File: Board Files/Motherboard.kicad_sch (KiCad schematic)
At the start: 121 parts, among them P1 72-Pin Connector, P2 EXP-Connector, P3 MOD RF, P4 Controller Input, P5 Controller Input, P6 PWR/RST IN, Q1 2SA937, Q2 2SC2021, Q3 2SC2021, U1 6116 (WRAM), U10 CIC, U2 74HC373, U3 74HC139, U4 6116 (VRAM), U5 RP2C02 PPU, U6 RP2A03 CPU, U7 40H368 (CI), U8 40H368 (CII), U9 74LS04, X1 21.477272 MHz, X2 4MHz

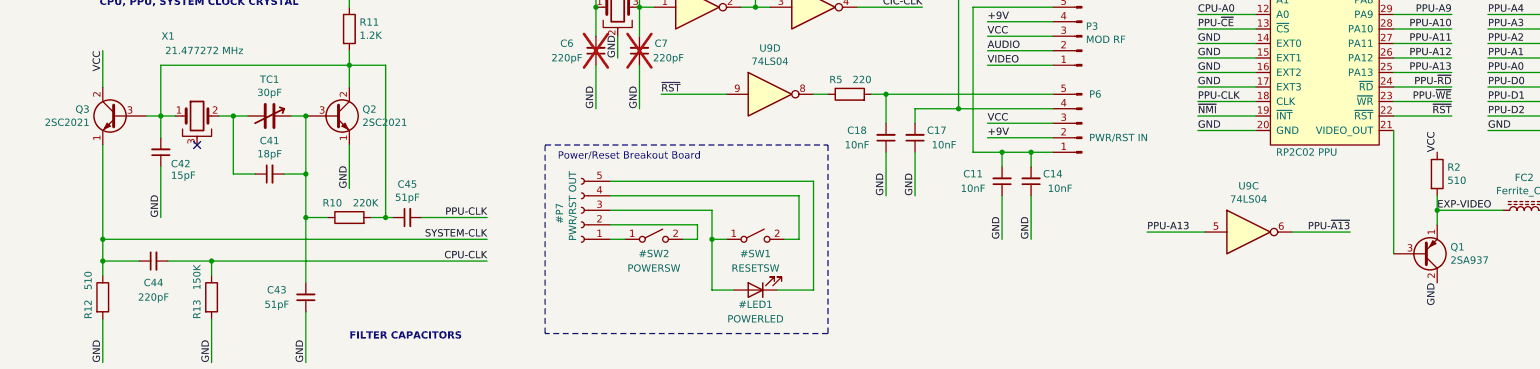
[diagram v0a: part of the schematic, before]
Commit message: fix: 74HC368 bus pin type
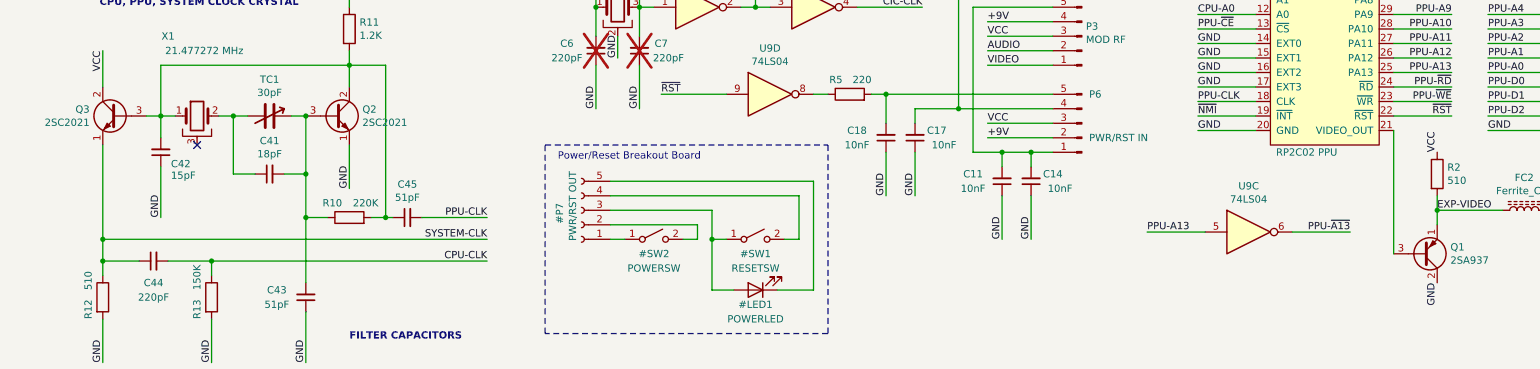
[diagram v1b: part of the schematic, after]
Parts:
- Q1: symbol Device:Q_PNP_ECB -> Transistor_BJT:Q_PNP_ECB
- Q2, Q3: symbol Device:Q_NPN_ECB -> Transistor_BJT:Q_NPN_ECB
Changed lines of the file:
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@@
 	)
 	(symbol
-		(lib_id "Device:Q_PNP_ECB")
+		(lib_id "Transistor_BJT:Q_PNP_ECB")
 		(at 267.97 215.9 0)
 		(mirror x)
@@
 			)
 		)
-		(property "Description" ""
+		(property "Description" "PNP transistor, emitter/collector/base"
 			(at 267.97 215.9 0)
 			(effects
@@
 	)
 	(symbol
-		(lib_id "Device:Q_NPN_ECB")
+		(lib_id "Transistor_BJT:Q_NPN_ECB")
 		(at 77.47 191.77 0)
 		(unit 1)
@@
 			)
 		)
-		(property "Description" ""
+		(property "Description" "NPN transistor, emitter/collector/base"
 			(at 77.47 191.77 0)
 			(effects
@@
 	)
 	(symbol
-		(lib_id "Device:Q_NPN_ECB")
+		(lib_id "Transistor_BJT:Q_NPN_ECB")
 		(at 39.37 191.77 0)
 		(mirror y)
@@
 			)
 		)
-		(property "Description" ""
+		(property "Description" "NPN transistor, emitter/collector/base"
 			(at 39.37 191.77 0)
 			(effects
@@
 			)
 		)
-		(property "Description" ""
+		(property "Description" "Light emitting diode"
+			(at 151.13 222.25 0)
+			(effects
+				(font
+					(size 1.27 1.27)
+				)
+				(hide yes)
+			)
+		)
+		(property "Sim.Pins" "1=K 2=A"
 			(at 151.13 222.25 0)
 			(effects

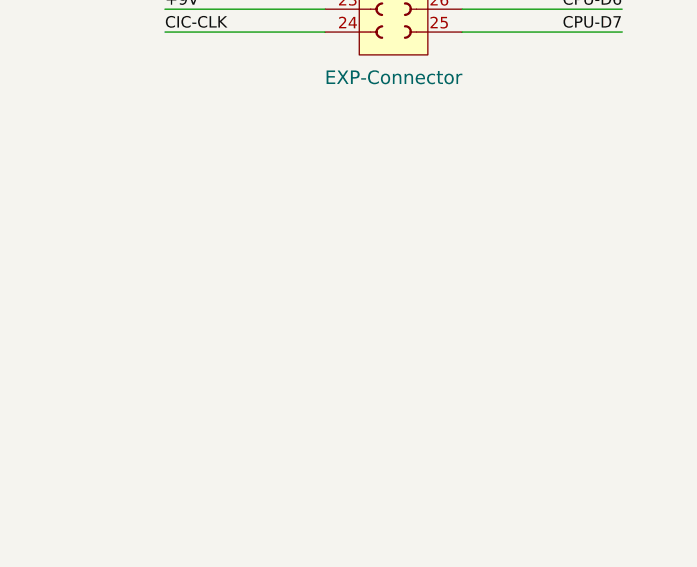
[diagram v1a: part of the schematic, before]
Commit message: feat: added power flag to gnd and vcc nets
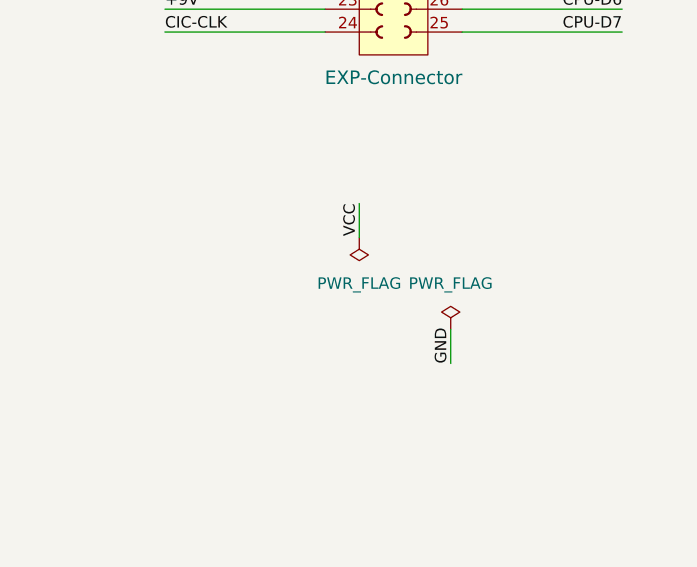
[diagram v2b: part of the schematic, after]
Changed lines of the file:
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@@
 	(wire
 		(pts
+			(xy 368.3 232.41) (xy 368.3 236.22)
+		)
+		(stroke
+			(width 0)
+			(type default)
+		)
+	)
+	(wire
+		(pts
 			(xy 369.57 199.39) (xy 387.35 199.39)
 		)
@@
 	(wire
 		(pts
+			(xy 358.14 218.44) (xy 358.14 222.25)
+		)
+		(stroke
+			(width 0)
+			(type default)
+		)
+	)
+	(wire
+		(pts
 			(xy 311.15 151.13) (xy 322.58 151.13)
 		)
@@
 		)
 	)
+	(label "VCC"
+		(at 358.14 218.44 270)
+		(effects
+			(font
+				(size 1.27 1.27)
+			)
+			(justify right bottom)
+		)
+	)
 	(label "CPU-A5"
 		(at 330.2 97.79 0)
@@
 	)
 	(label "GND"
+		(at 368.3 236.22 90)
+		(effects
+			(font
+				(size 1.27 1.27)
+			)
+			(justify left bottom)
+		)
+	)
+	(label "GND"
 		(at 134.62 107.95 90)
 		(effects
@@
 				)
 			)
+		)
+	)
+	(symbol
+		(lib_id "power:PWR_FLAG")
+		(at 358.14 222.25 180)
+		(unit 1)
+		(exclude_from_sim no)
+		(in_bom yes)
+		(on_board yes)
+		(dnp no)
+		(fields_autoplaced yes)
+		(property "Reference" "#FLG01"
+			(at 358.14 224.155 0)
+			(effects
+				(font
+					(size 1.27 1.27)
+				)
+				(hide yes)
+			)
+		)
+		(property "Value" "PWR_FLAG"
+			(at 358.14 227.33 0)
+			(effects
+				(font
+					(size 1.27 1.27)
+				)
+			)
+		)
+		(property "Footprint" ""
+			(at 358.14 222.25 0)
+			(effects
+				(font
+					(size 1.27 1.27)
+				)
+				(hide yes)
+			)
+		)
+		(property "Datasheet" "~"
+			(at 358.14 222.25 0)
+			(effects
+				(font
+					(size 1.27 1.27)
+				)
+				(hide yes)
+			)
+		)
+		(property "Description" "Special symbol for telling ERC where power comes from"
+			(at 358.14 222.25 0)
+			(effects
+				(font
+					(size 1.27 1.27)
+				)
+				(hide yes)
+			)
+		)
+		(pin "1"
+		)
+		(instances
+			(project ""
+				(path "/d10b47ec-15d7-4098-8a2a-c0827f933fba"
+					(reference "#FLG01")
+					(unit 1)
+				)
+			)
+		)
+	)
+	(symbol
+		(lib_id "power:PWR_FLAG")
+		(at 368.3 232.41 0)
+		(unit 1)
+		(exclude_from_sim no)
+		(in_bom yes)
+		(on_board yes)
+		(dnp no)
+		(fields_autoplaced yes)
+		(property "Reference" "#FLG02"
+			(at 368.3 230.505 0)
+			(effects
+				(font
+					(size 1.27 1.27)
+				)
+				(hide yes)
+			)
+		)
+		(property "Value" "PWR_FLAG"
+			(at 368.3 227.33 0)
+			(effects
+				(font
+					(size 1.27 1.27)
+				)
+			)
+		)
+		(property "Footprint" ""
+			(at 368.3 232.41 0)
+			(effects
+				(font
+					(size 1.27 1.27)
+				)
+				(hide yes)
+			)
+		)
+		(property "Datasheet" "~"
+			(at 368.3 232.41 0)
+			(effects
+				(font
+					(size 1.27 1.27)
+				)
+				(hide yes)
+			)
+		)
+		(property "Description" "Special symbol for telling ERC where power comes from"
+			(at 368.3 232.41 0)
+			(effects
+				(font
+					(size 1.27 1.27)
+				)
+				(hide yes)
+			)
+		)
+		(pin "1"
+		)
+		(instances
+			(project ""
+				(path "/d10b47ec-15d7-4098-8a2a-c0827f933fba"
+					(reference "#FLG02")
+					(unit 1)
+				)
+			)
